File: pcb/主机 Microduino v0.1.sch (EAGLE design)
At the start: 13 parts, among them IC1 ASM1117, IC2 ASM1117, J1 DCJ0202

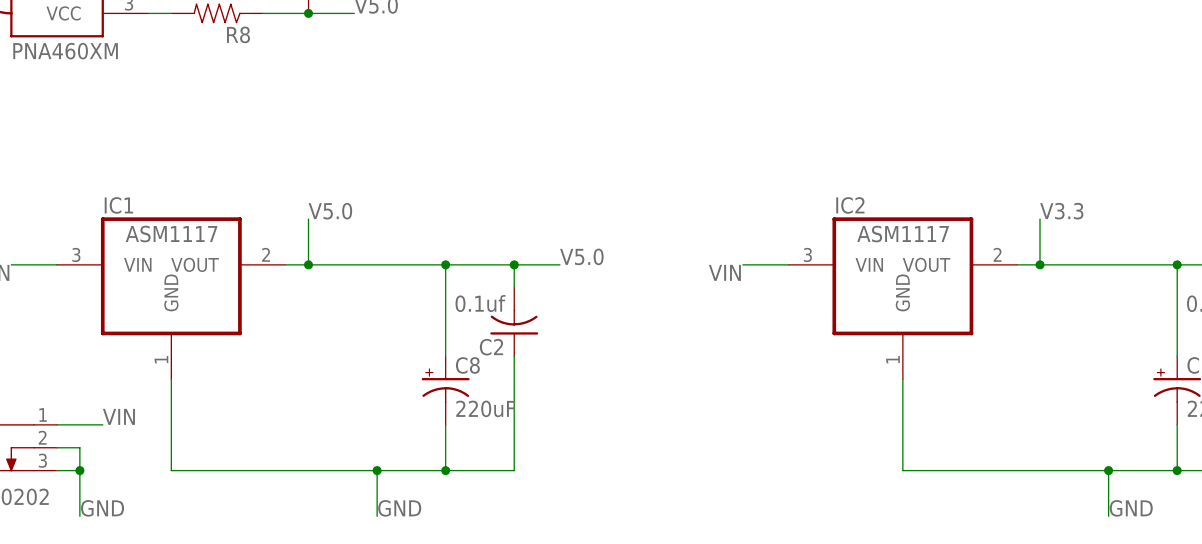
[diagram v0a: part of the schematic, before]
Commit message: 更新了Microduino面包版PCB
更新了Microduino面包版PCB
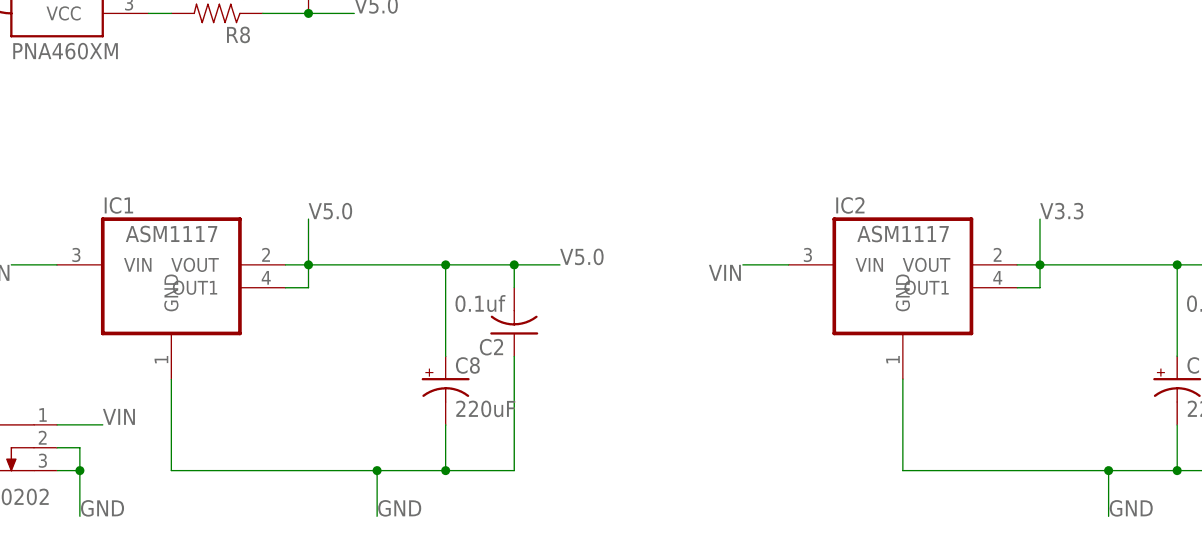
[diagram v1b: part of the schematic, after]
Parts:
- IC1, IC2: device burr-brown:REG1117 -> MY3:ASM1117
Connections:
- net V3.3: now also IC2.OUT1
- net V5.0: now also IC1.OUT1
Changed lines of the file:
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@@
 <grid distance="0.1" unitdist="inch" unit="inch" style="lines" multiple="1" display="no" altdistance="0.01" altunitdist="inch" altunit="inch"/>
 <layers>
-<layer number="1" name="Top" color="4" fill="1" visible="yes" active="no"/>
-<layer number="2" name="Route2" color="1" fill="3" visible="yes" active="no"/>
-<layer number="3" name="Route3" color="4" fill="3" visible="yes" active="no"/>
-<layer number="4" name="Route4" color="1" fill="4" visible="yes" active="no"/>
-<layer number="5" name="Route5" color="4" fill="4" visible="yes" active="no"/>
-<layer number="6" name="Route6" color="1" fill="8" visible="yes" active="no"/>
-<layer number="7" name="Route7" color="4" fill="8" visible="yes" active="no"/>
-<layer number="8" name="Route8" color="1" fill="2" visible="yes" active="no"/>
-<layer number="9" name="Route9" color="4" fill="2" visible="yes" active="no"/>
-<layer number="10" name="Route10" color="1" fill="7" visible="yes" active="no"/>
-<layer number="11" name="Route11" color="4" fill="7" visible="yes" active="no"/>
-<layer number="12" name="Route12" color="1" fill="5" visible="yes" active="no"/>
-<layer number="13" name="Route13" color="4" fill="5" visible="yes" active="no"/>
-<layer number="14" name="Route14" color="1" fill="6" visible="yes" active="no"/>
-<layer number="15" name="Route15" color="4" fill="6" visible="yes" active="no"/>
-<layer number="16" name="Bottom" color="1" fill="1" visible="yes" active="no"/>
-<layer number="17" name="Pads" color="2" fill="1" visible="yes" active="no"/>
-<layer number="18" name="Vias" color="2" fill="1" visible="yes" active="no"/>
-<layer number="19" name="Unrouted" color="6" fill="1" visible="yes" active="no"/>
-<layer number="20" name="Dimension" color="15" fill="1" visible="yes" active="no"/>
-<layer number="21" name="tPlace" color="7" fill="1" visible="yes" active="no"/>
-<layer number="22" name="bPlace" color="7" fill="1" visible="yes" active="no"/>
-<layer number="23" name="tOrigins" color="15" fill="1" visible="yes" active="no"/>
-<layer number="24" name="bOrigins" color="15" fill="1" visible="yes" active="no"/>
-<layer number="25" name="tNames" color="7" fill="1" visible="yes" active="no"/>
-<layer number="26" name="bNames" color="7" fill="1" visible="yes" active="no"/>
-<layer number="27" name="tValues" color="7" fill="1" visible="yes" active="no"/>
-<layer number="28" name="bValues" color="7" fill="1" visible="yes" active="no"/>
+<layer number="1" name="Top" color="4" fill="1" visible="no" active="no"/>
+<layer number="2" name="Route2" color="1" fill="3" visible="no" active="no"/>
+<layer number="3" name="Route3" color="4" fill="3" visible="no" active="no"/>
+<layer number="4" name="Route4" color="1" fill="4" visible="no" active="no"/>
+<layer number="5" name="Route5" color="4" fill="4" visible="no" active="no"/>
+<layer number="6" name="Route6" color="1" fill="8" visible="no" active="no"/>
+<layer number="7" name="Route7" color="4" fill="8" visible="no" active="no"/>
+<layer number="8" name="Route8" color="1" fill="2" visible="no" active="no"/>
+<layer number="9" name="Route9" color="4" fill="2" visible="no" active="no"/>
+<layer number="10" name="Route10" color="1" fill="7" visible="no" active="no"/>
+<layer number="11" name="Route11" color="4" fill="7" visible="no" active="no"/>
+<layer number="12" name="Route12" color="1" fill="5" visible="no" active="no"/>
+<layer number="13" name="Route13" color="4" fill="5" visible="no" active="no"/>
+<layer number="14" name="Route14" color="1" fill="6" visible="no" active="no"/>
+<layer number="15" name="Route15" color="4" fill="6" visible="no" active="no"/>
+<layer number="16" name="Bottom" color="1" fill="1" visible="no" active="no"/>
+<layer number="17" name="Pads" color="2" fill="1" visible="no" active="no"/>
+<layer number="18" name="Vias" color="2" fill="1" visible="no" active="no"/>
+<layer number="19" name="Unrouted" color="6" fill="1" visible="no" active="no"/>
+<layer number="20" name="Dimension" color="15" fill="1" visible="no" active="no"/>
+<layer number="21" name="tPlace" color="7" fill="1" visible="no" active="no"/>
+<layer number="22" name="bPlace" color="7" fill="1" visible="no" active="no"/>
+<layer number="23" name="tOrigins" color="15" fill="1" visible="no" active="no"/>
+<layer number="24" name="bOrigins" color="15" fill="1" visible="no" active="no"/>
+<layer number="25" name="tNames" color="7" fill="1" visible="no" active="no"/>
+<layer number="26" name="bNames" color="7" fill="1" visible="no" active="no"/>
+<layer number="27" name="tValues" color="7" fill="1" visible="no" active="no"/>
+<layer number="28" name="bValues" color="7" fill="1" visible="no" active="no"/>
 <layer number="29" name="tStop" color="7" fill="3" visible="no" active="no"/>
 <layer number="30" name="bStop" color="7" fill="6" visible="no" active="no"/>
@@
 <layer number="35" name="tGlue" color="7" fill="4" visible="no" active="no"/>
 <layer number="36" name="bGlue" color="7" fill="5" visible="no" active="no"/>
-<layer number="37" name="tTest" color="7" fill="1" visible="yes" active="no"/>
-<layer number="38" name="bTest" color="7" fill="1" visible="yes" active="no"/>
+<layer number="37" name="tTest" color="7" fill="1" visible="no" active="no"/>
+<layer number="38" name="bTest" color="7" fill="1" visible="no" active="no"/>
 <layer number="39" name="tKeepout" color="4" fill="11" visible="no" active="no"/>
 <layer number="40" name="bKeepout" color="1" fill="11" visible="no" active="no"/>
@@
 <layer number="44" name="Drills" color="7" fill="1" visible="no" active="no"/>
 <layer number="45" name="Holes" color="7" fill="1" visible="no" active="no"/>
-<layer number="46" name="Milling" color="3" fill="1" visible="yes" active="no"/>
-<layer number="47" name="Measures" color="7" fill="1" visible="yes" active="no"/>
-<layer number="48" name="Document" color="7" fill="1" visible="yes" active="no"/>
-<layer number="49" name="Reference" color="7" fill="1" visible="yes" active="no"/>
-<layer number="50" name="dxf" color="7" fill="1" visible="yes" active="no"/>
-<layer number="51" name="tDocu" color="7" fill="1" visible="yes" active="no"/>
-<layer number="52" name="bDocu" color="7" fill="1" visible="yes" active="no"/>
-<layer number="53" name="tGND_GNDA" color="7" fill="9" visible="yes" active="no"/>
-<layer number="54" name="bGND_GNDA" color="1" fill="9" visible="yes" active="no"/>
-<layer number="56" name="wert" color="7" fill="1" visible="yes" active="no"/>
+<layer number="46" name="Milling" color="3" fill="1" visible="no" active="no"/>
+<layer number="47" name="Measures" color="7" fill="1" visible="no" active="no"/>
+<layer number="48" name="Document" color="7" fill="1" visible="no" active="no"/>
+<layer number="49" name="Reference" color="7" fill="1" visible="no" active="no"/>
+<layer number="50" name="dxf" color="7" fill="1" visible="no" active="no"/>
+<layer number="51" name="tDocu" color="7" fill="1" visible="no" active="no"/>
+<layer number="52" name="bDocu" color="7" fill="1" visible="no" active="no"/>
+<layer number="53" name="tGND_GNDA" color="7" fill="9" visible="no" active="no"/>
+<layer number="54" name="bGND_GNDA" color="1" fill="9" visible="no" active="no"/>
+<layer number="56" name="wert" color="7" fill="1" visible="no" active="no"/>
 <layer number="91" name="Nets" color="2" fill="1" visible="yes" active="yes"/>
 <layer number="92" name="Busses" color="1" fill="1" visible="yes" active="yes"/>
@@
 <parts>
 <part name="U$1" library="MY2" deviceset="PING-MICRDUINO-DZ" device="/1009"/>
-<part name="IC1" library="burr-brown" deviceset="REG1117" device="" value="ASM1117"/>
+<part name="IC1" library="MY3" deviceset="ASM1117" device="" value="ASM1117"/>
 <part name="C8" library="resistor" deviceset="CPOL-US" device="E2.5-5" value="220uF"/>
 <part name="J1" library="con-jack" deviceset="DCJ0202" device=""/>
@@
 <part name="R8" library="MY" deviceset="RESISTOR" device="PTH1" value="49.9"/>
 <part name="JP1" library="pinhead" deviceset="PINHD-1X4" device=""/>
-<part name="IC2" library="burr-brown" deviceset="REG1117" device="" value="ASM1117"/>
+<part name="IC2" library="MY3" deviceset="ASM1117" device="" value="ASM1117"/>
 <part name="C1" library="resistor" deviceset="CPOL-US" device="E2.5-5" value="220uF"/>
 <part name="C3" library="resistor" deviceset="C-US" device="025-024X044" value="0.1uf"/>
@@
 <junction x="142.24" y="27.94"/>
 <wire x1="157.48" y1="27.94" x2="142.24" y2="27.94" width="0.1524" layer="91"/>
+<pinref part="IC1" gate="G$1" pin="OUT1"/>
+<wire x1="139.7" y1="25.4" x2="142.24" y2="25.4" width="0.1524" layer="91"/>
+<wire x1="142.24" y1="25.4" x2="142.24" y2="27.94" width="0.1524" layer="91"/>
 </segment>
 <segment>
@@
 <junction x="223.52" y="27.94"/>
 <wire x1="238.76" y1="27.94" x2="223.52" y2="27.94" width="0.1524" layer="91"/>
-</segment>
-<segment>
+<pinref part="IC2" gate="G$1" pin="OUT1"/>
+<wire x1="220.98" y1="25.4" x2="223.52" y2="25.4" width="0.1524" layer="91"/>
+<wire x1="223.52" y1="25.4" x2="223.52" y2="27.94" width="0.1524" layer="91"/>
+</segment>
+<segment>
